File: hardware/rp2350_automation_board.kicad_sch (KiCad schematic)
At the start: 0 parts

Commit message: Board complete
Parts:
- added D1: MBR230S1F-7, Samacsys:SODFL3518X115N, symbol Samacsys:MBR230S1F-7
- added J1, J2: PH1-20-UA, Samacsys:HDRV20W64P0X254_1X20_5080X249X886P, symbol Samacsys:PH1-20-UA
- added U1: Pico, RP-Pico Libraries:RPi_Pico_SMD_TH, symbol RP_Pico:Pico
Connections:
- new net: J1.1, U1.1 (GPIO0)
- new net: J1.11, U1.11 (GPIO8)
- new net: J1.12, U1.12 (GPIO9)
- new net: J1.14, U1.14 (GPIO10)
- new net: J1.19, U1.19 (GPIO14)
- new net: J1.2, U1.2 (GPIO1)
- new net: J1.20, U1.20 (GPIO15)
- new net: J2.14, U1.27 (GPIO21)
- new net: J2.12, U1.29 (GPIO22)
- new net: J2.11, U1.30 (RUN)
- new net: J2.7, U1.34 (GPIO28_ADC2)
- new net: J2.6, U1.35 (ADC_VREF)
- new net: J2.4, U1.37 (3V3_EN)
- new net: D1.1 (K), U1.39 (VSYS)
- new net +3V3: J2.5, U1.36 (3V3)
- new net +5V: D1.2 (A), J2.2
- new net ADC0: J2.10, U1.31 (GPIO26_ADC0)
- new net ADC1: J2.9, U1.32 (GPIO27_ADC1)
- new net DAC_RESET: J2.15, U1.26 (GPIO20)
- new net DIN_1: J1.7, U1.7 (GPIO5)
- new net DIN_2: J1.9, U1.9 (GPIO6)
- new net DIN_3: J1.10, U1.10 (GPIO7)
- new net DOUT_1: J1.4, U1.4 (GPIO2)
- new net DOUT_2: J1.5, U1.5 (GPIO3)
- new net DOUT_3: J1.6, U1.6 (GPIO4)
- new net GND: J1.13, J1.18, J1.3, J1.8, J2.13, J2.18, J2.3, J2.8, U1.13 (GND), U1.18 (GND), U1.23 (GND), U1.28 (GND), U1.3 (GND), U1.33 (AGND), U1.38 (GND), U1.8 (GND)
- new net RS485_MODE: J1.15, U1.15 (GPIO11)
- new net SPI0_CS: J2.19, U1.22 (GPIO17)
- new net SPI0_MISO: J2.20, U1.21 (GPIO16)
- new net SPI0_MOSI: J2.16, U1.25 (GPIO19)
- new net SPI0_SCK: J2.17, U1.24 (GPIO18)
- new net UART_RX: J1.17, U1.17 (GPIO13)
- new net UART_TX: J1.16, U1.16 (GPIO12)
- no-connect marks 0 -> 5
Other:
- removed sheet MCU

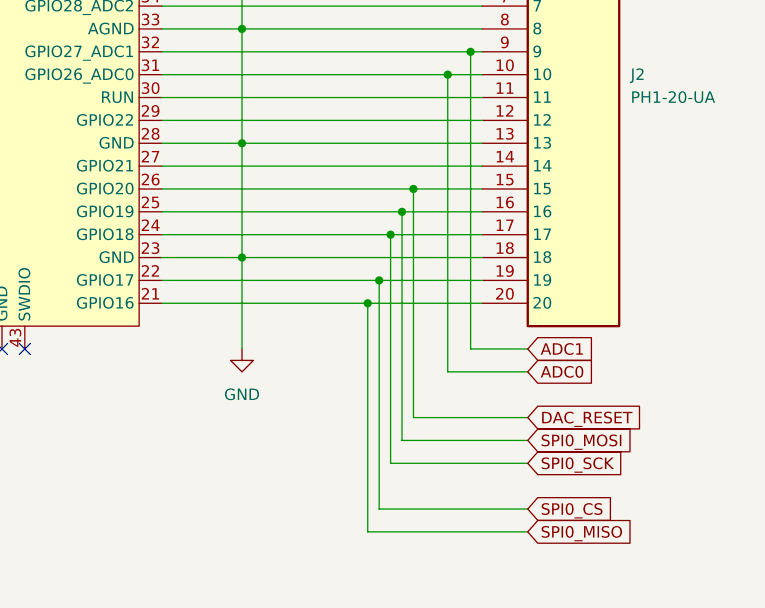
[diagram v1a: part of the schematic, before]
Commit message: LDAC added
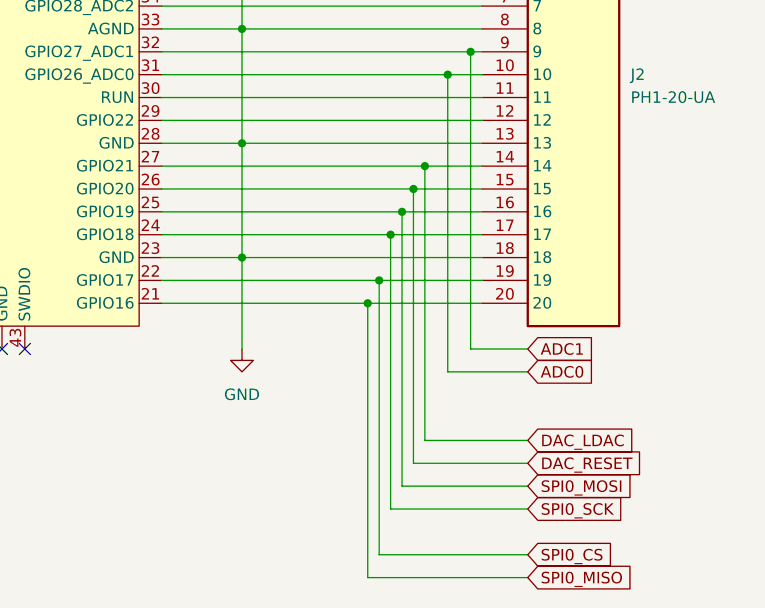
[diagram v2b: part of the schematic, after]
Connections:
- net DAC_LDAC: now reaches J2.14, U1.27 (GPIO21)
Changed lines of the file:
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@@
+	)
+	(junction
+		(at 133.35 102.87)
+		(diameter 0)
+		(color 0 0 0 0)
 	)
 	(junction
@@
 	(wire
 		(pts
-			(xy 128.27 140.97) (xy 128.27 115.57)
+			(xy 128.27 146.05) (xy 128.27 115.57)
 		)
 		(stroke
@@
 	(wire
 		(pts
-			(xy 104.14 102.87) (xy 139.7 102.87)
+			(xy 104.14 102.87) (xy 133.35 102.87)
 		)
 		(stroke
@@
 	(wire
 		(pts
-			(xy 129.54 135.89) (xy 129.54 110.49)
+			(xy 129.54 140.97) (xy 129.54 110.49)
 		)
 		(stroke
@@
 	(wire
 		(pts
-			(xy 130.81 133.35) (xy 130.81 107.95)
+			(xy 130.81 138.43) (xy 130.81 107.95)
 		)
 		(stroke
@@
 	(wire
 		(pts
-			(xy 128.27 140.97) (xy 144.78 140.97)
+			(xy 128.27 146.05) (xy 144.78 146.05)
 		)
 		(stroke
@@
 	(wire
 		(pts
+			(xy 133.35 133.35) (xy 133.35 102.87)
+		)
+		(stroke
+			(width 0)
+			(type default)
+		)
+	)
+	(wire
+		(pts
 			(xy 104.14 85.09) (xy 139.7 85.09)
 		)
@@
 	(wire
 		(pts
-			(xy 130.81 133.35) (xy 144.78 133.35)
+			(xy 130.81 138.43) (xy 144.78 138.43)
 		)
 		(stroke
@@
 	(wire
 		(pts
+			(xy 133.35 102.87) (xy 139.7 102.87)
+		)
+		(stroke
+			(width 0)
+			(type default)
+		)
+	)
+	(wire
+		(pts
 			(xy 113.03 74.93) (xy 139.7 74.93)
 		)
@@
 	(wire
 		(pts
-			(xy 127 143.51) (xy 144.78 143.51)
+			(xy 127 148.59) (xy 144.78 148.59)
 		)
 		(stroke
@@
 	(wire
 		(pts
-			(xy 132.08 130.81) (xy 132.08 105.41)
+			(xy 132.08 135.89) (xy 132.08 105.41)
+		)
+		(stroke
+			(width 0)
+			(type default)
+		)
+	)
+	(wire
+		(pts
+			(xy 144.78 133.35) (xy 133.35 133.35)
 		)
 		(stroke
@@
 	(wire
 		(pts
-			(xy 132.08 130.81) (xy 144.78 130.81)
+			(xy 132.08 135.89) (xy 144.78 135.89)
 		)
 		(stroke
@@
 	(wire
 		(pts
-			(xy 129.54 135.89) (xy 144.78 135.89)
+			(xy 129.54 140.97) (xy 144.78 140.97)
 		)
 		(stroke
@@
 	(wire
 		(pts
-			(xy 127 143.51) (xy 127 118.11)
+			(xy 127 148.59) (xy 127 118.11)
 		)
 		(stroke
@@
 	(global_label "DAC_RESET"
 		(shape input)
-		(at 144.78 130.81 0)
+		(at 144.78 135.89 0)
 		(fields_autoplaced yes)
 		(effects
@@
 		)
 		(property "Intersheetrefs" "${INTERSHEET_REFS}"
-			(at 158.1065 130.81 0)
+			(at 158.1065 135.89 0)
 			(effects
 				(font
@@
 	(global_label "SPI0_CS"
 		(shape input)
-		(at 144.78 140.97 0)
+		(at 144.78 146.05 0)
 		(fields_autoplaced yes)
 		(effects
@@
 		)
 		(property "Intersheetrefs" "${INTERSHEET_REFS}"
-			(at 155.5061 140.97 0)
+			(at 155.5061 146.05 0)
 			(effects
 				(font
@@
 	(global_label "SPI0_MISO"
 		(shape input)
-		(at 144.78 143.51 0)
+		(at 144.78 148.59 0)
 		(fields_autoplaced yes)
 		(effects
@@
 		)
 		(property "Intersheetrefs" "${INTERSHEET_REFS}"
-			(at 157.6228 143.51 0)
+			(at 157.6228 148.59 0)
 			(effects
 				(font
@@
 		)
 	)
+	(global_label "DAC_LDAC"
+		(shape input)
+		(at 144.78 133.35 0)
+		(fields_autoplaced yes)
+		(effects
+			(font
+				(size 1.27 1.27)
+			)
+			(justify left)
+		)
+		(property "Intersheetrefs" "${INTERSHEET_REFS}"
+			(at 157.0181 133.35 0)
+			(effects
+				(font
+					(size 1.27 1.27)
+				)
+				(justify left)
+				(hide yes)
+			)
+		)
+	)
 	(global_label "DOUT_2"
 		(shape input)
@@
 	(global_label "SPI0_MOSI"
 		(shape input)
-		(at 144.78 133.35 0)
+		(at 144.78 138.43 0)
 		(fields_autoplaced yes)
 		(effects
@@
 		)
 		(property "Intersheetrefs" "${INTERSHEET_REFS}"
-			(at 157.6228 133.35 0)
+			(at 157.6228 138.43 0)
 			(effects
 				(font
@@
 	(global_label "SPI0_SCK"
 		(shape input)
-		(at 144.78 135.89 0)
+		(at 144.78 140.97 0)
 		(fields_autoplaced yes)
 		(effects
@@
 		)
 		(property "Intersheetrefs" "${INTERSHEET_REFS}"
-			(at 156.7761 135.89 0)
-			(effects
-				(font
+			(at 156.7761 140.97 0)
+			(effects
+				(font

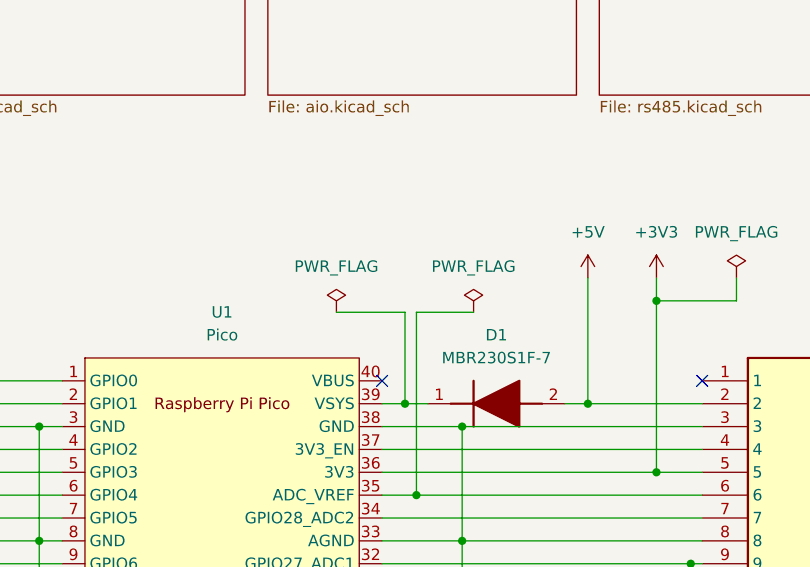
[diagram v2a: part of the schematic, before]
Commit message: Modbus, small schematic changes
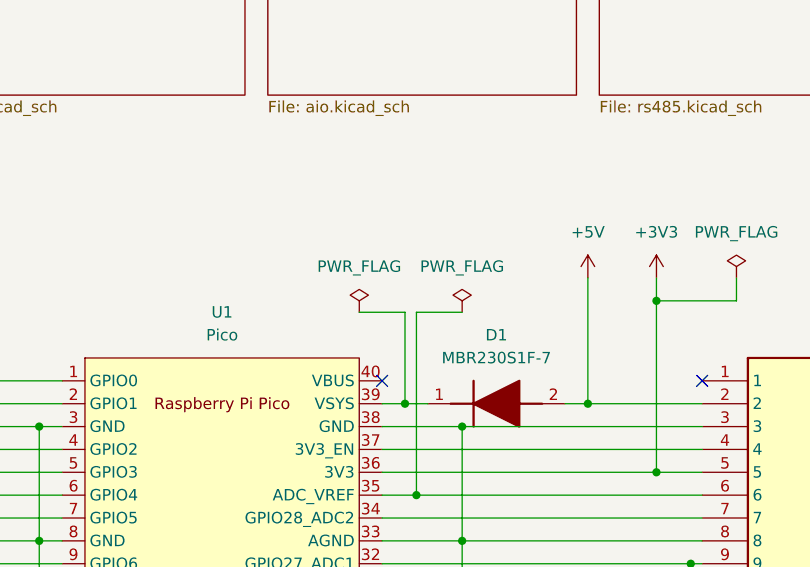
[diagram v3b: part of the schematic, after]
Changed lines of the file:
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@@
 	(wire
 		(pts
-			(xy 99.06 62.23) (xy 106.68 62.23)
+			(xy 101.6 62.23) (xy 106.68 62.23)
 		)
 		(stroke
@@
 	(wire
 		(pts
-			(xy 107.95 62.23) (xy 114.3 62.23)
+			(xy 107.95 62.23) (xy 113.03 62.23)
 		)
 		(stroke
@@
 	(symbol
 		(lib_id "power:PWR_FLAG")
-		(at 114.3 62.23 0)
+		(at 113.03 62.23 0)
 		(unit 1)
 		(exclude_from_sim no)
@@
 		(fields_autoplaced yes)
 		(property "Reference" "#FLG05"
-			(at 114.3 60.325 0)
+			(at 113.03 60.325 0)
 			(effects
 				(font
@@
 		)
 		(property "Value" "PWR_FLAG"
-			(at 114.3 57.15 0)
+			(at 113.03 57.15 0)
 			(effects
 				(font
@@
 		)
 		(property "Footprint" ""
-			(at 114.3 62.23 0)
+			(at 113.03 62.23 0)
 			(effects
 				(font
@@
 		)
 		(property "Datasheet" "~"
-			(at 114.3 62.23 0)
+			(at 113.03 62.23 0)
 			(effects
 				(font
@@
 		)
 		(property "Description" "Special symbol for telling ERC where power comes from"
-			(at 114.3 62.23 0)
+			(at 113.03 62.23 0)
 			(effects
 				(font
@@
 	(symbol
 		(lib_id "power:PWR_FLAG")
-		(at 99.06 62.23 0)
+		(at 101.6 62.23 0)
 		(unit 1)
 		(exclude_from_sim no)
@@
 		(fields_autoplaced yes)
 		(property "Reference" "#FLG01"
-			(at 99.06 60.325 0)
+			(at 101.6 60.325 0)
 			(effects
 				(font
@@
 		)
 		(property "Value" "PWR_FLAG"
-			(at 99.06 57.15 0)
+			(at 101.6 57.15 0)
 			(effects
 				(font
@@
 		)
 		(property "Footprint" ""
-			(at 99.06 62.23 0)
+			(at 101.6 62.23 0)
 			(effects
 				(font
@@
 		)
 		(property "Datasheet" "~"
-			(at 99.06 62.23 0)
+			(at 101.6 62.23 0)
 			(effects
 				(font
@@
 		)
 		(property "Description" "Special symbol for telling ERC where power comes from"
-			(at 99.06 62.23 0)
-			(effects
-				(font
+			(at 101.6 62.23 0)
+			(effects
+				(font

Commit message: UART parity and better timing handling
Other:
- title: (none) -> Microcontroller RP2350
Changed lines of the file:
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@@
 	(generator_version "9.0")
 	(paper "A4")
+	(title_block
+		(title "Microcontroller RP2350")
+	)
 	(junction
 		(at 128.27 115.57)
